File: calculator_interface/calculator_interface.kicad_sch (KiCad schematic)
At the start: 8 parts, among them J1 Conn_02x08_Interface_Side, J2 Conn_02x20_TI30XA, U1 MCP1700-1502E/TO

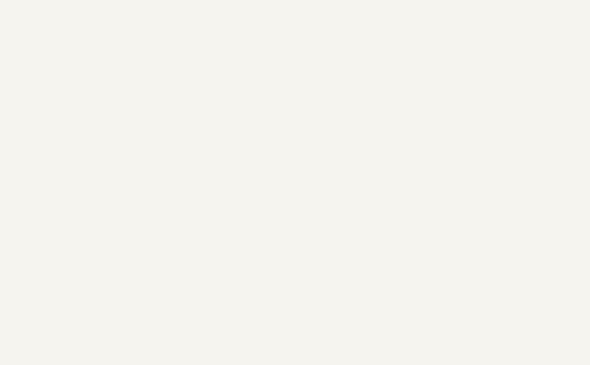
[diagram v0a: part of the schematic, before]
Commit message: add mounting holes
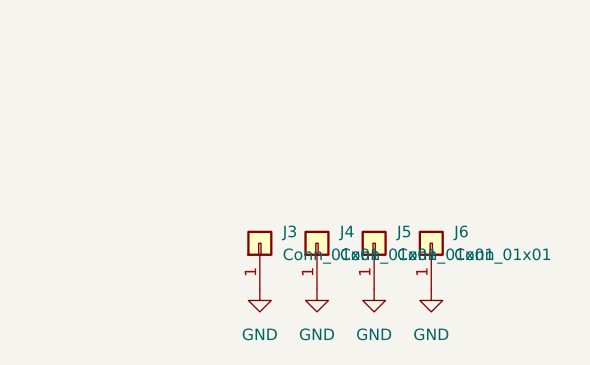
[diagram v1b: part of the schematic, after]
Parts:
- added J3, J4, J5, J6: Conn_01x01, MountingHole:MountingHole_5mm_Pad_Via, symbol Connector_Generic:Conn_01x01
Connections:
- net GND: now also J3.1 (Pin_1), J4.1 (Pin_1), J5.1 (Pin_1), J6.1 (Pin_1)
